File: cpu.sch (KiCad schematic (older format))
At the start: 28 parts, among them P27 BDM, U1 MC9S12XDP512, X1 16MHz

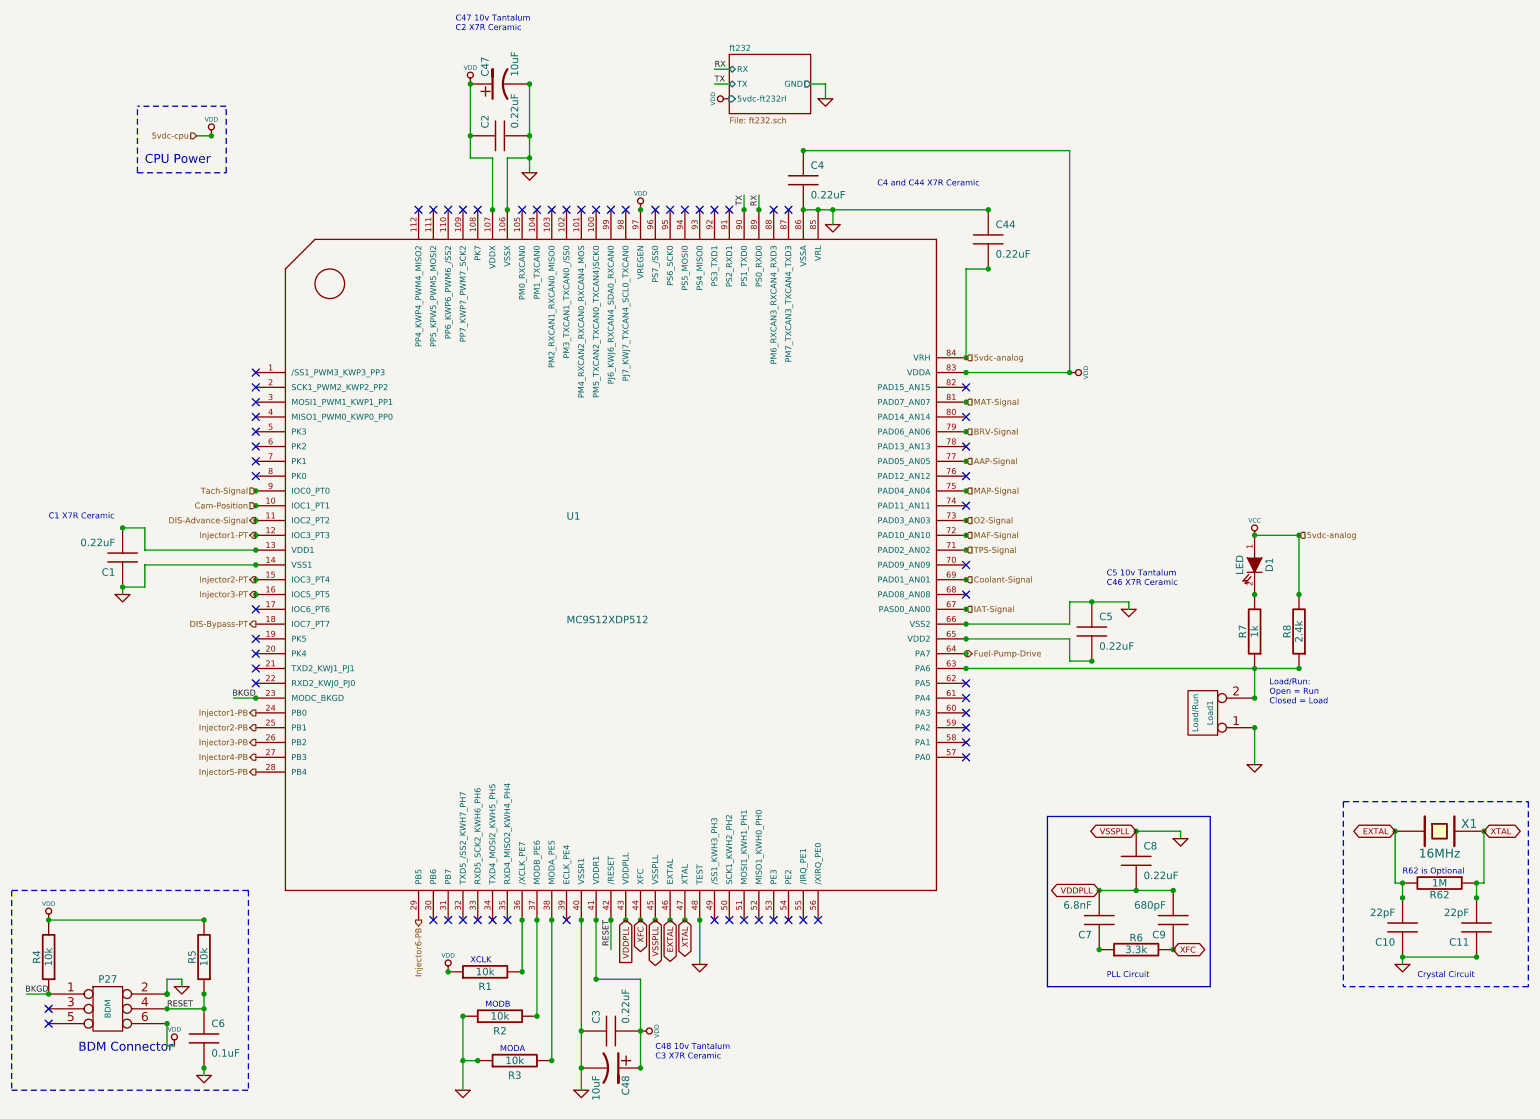
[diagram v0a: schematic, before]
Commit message: Updated Schematics, PDF, BOM for 4cyl Sequential Injection
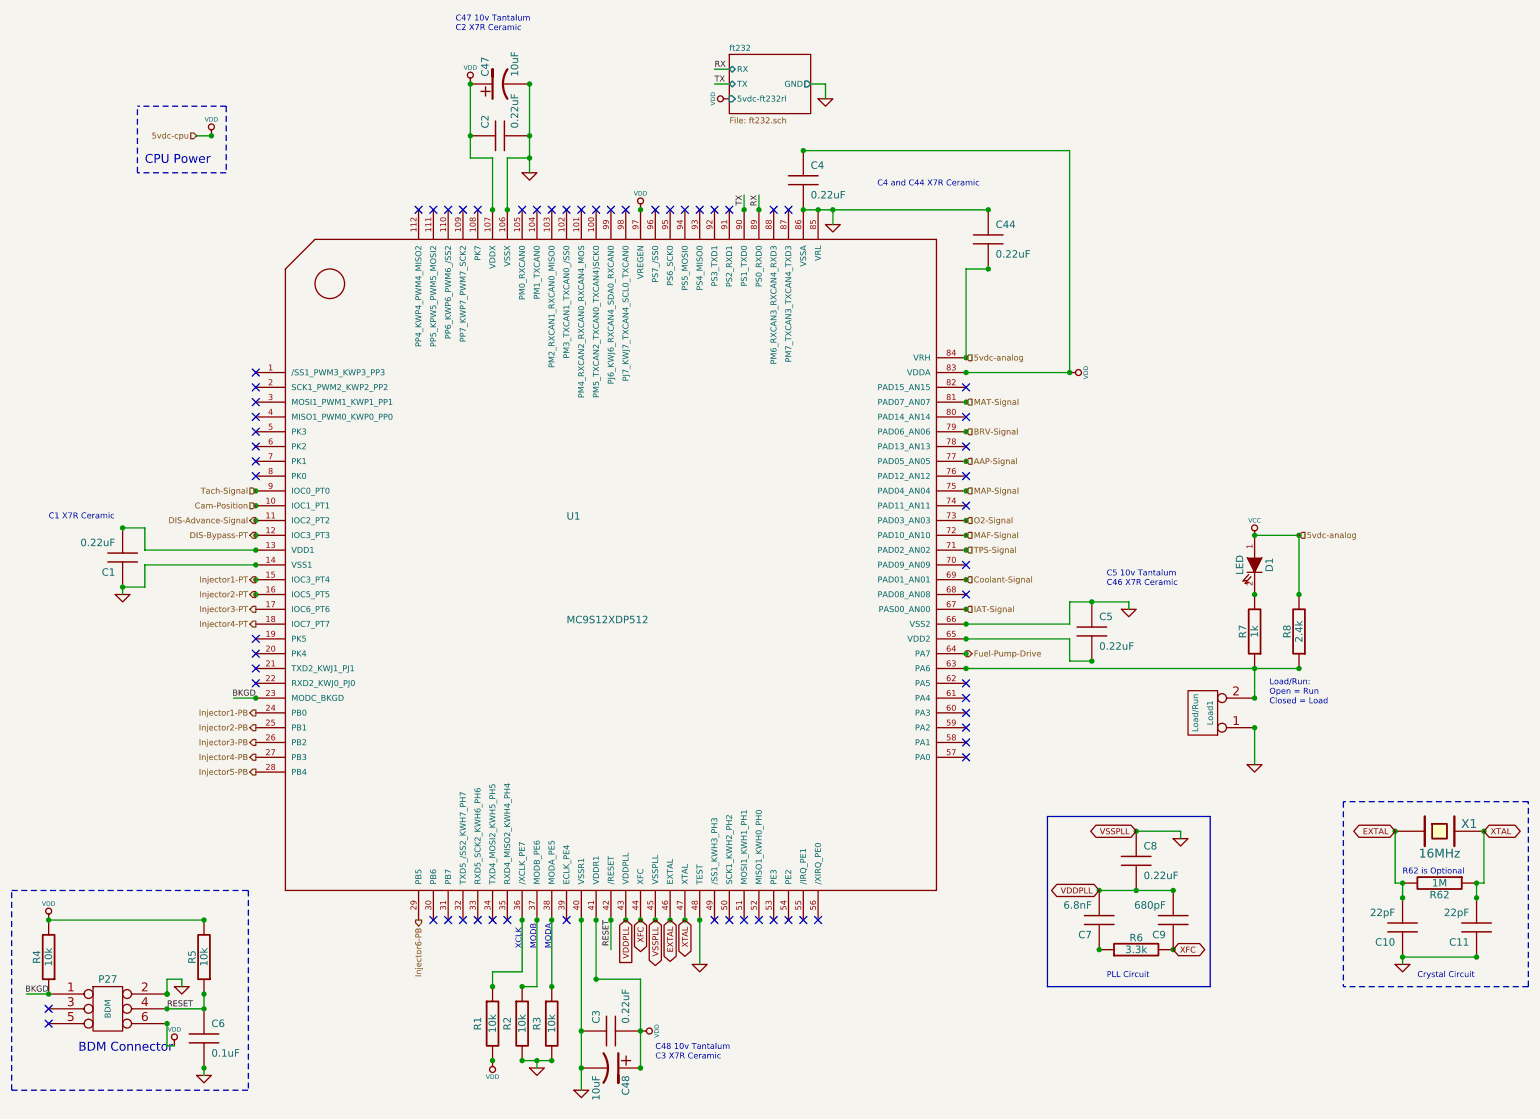
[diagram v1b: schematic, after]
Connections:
- net labels added: Injector4-PT
- wire segments 72 -> 75
- no-connect marks 64 -> 63
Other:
- moved on the sheet: R1, R2, R3

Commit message: Updated everything for up to 8 cylinder engines
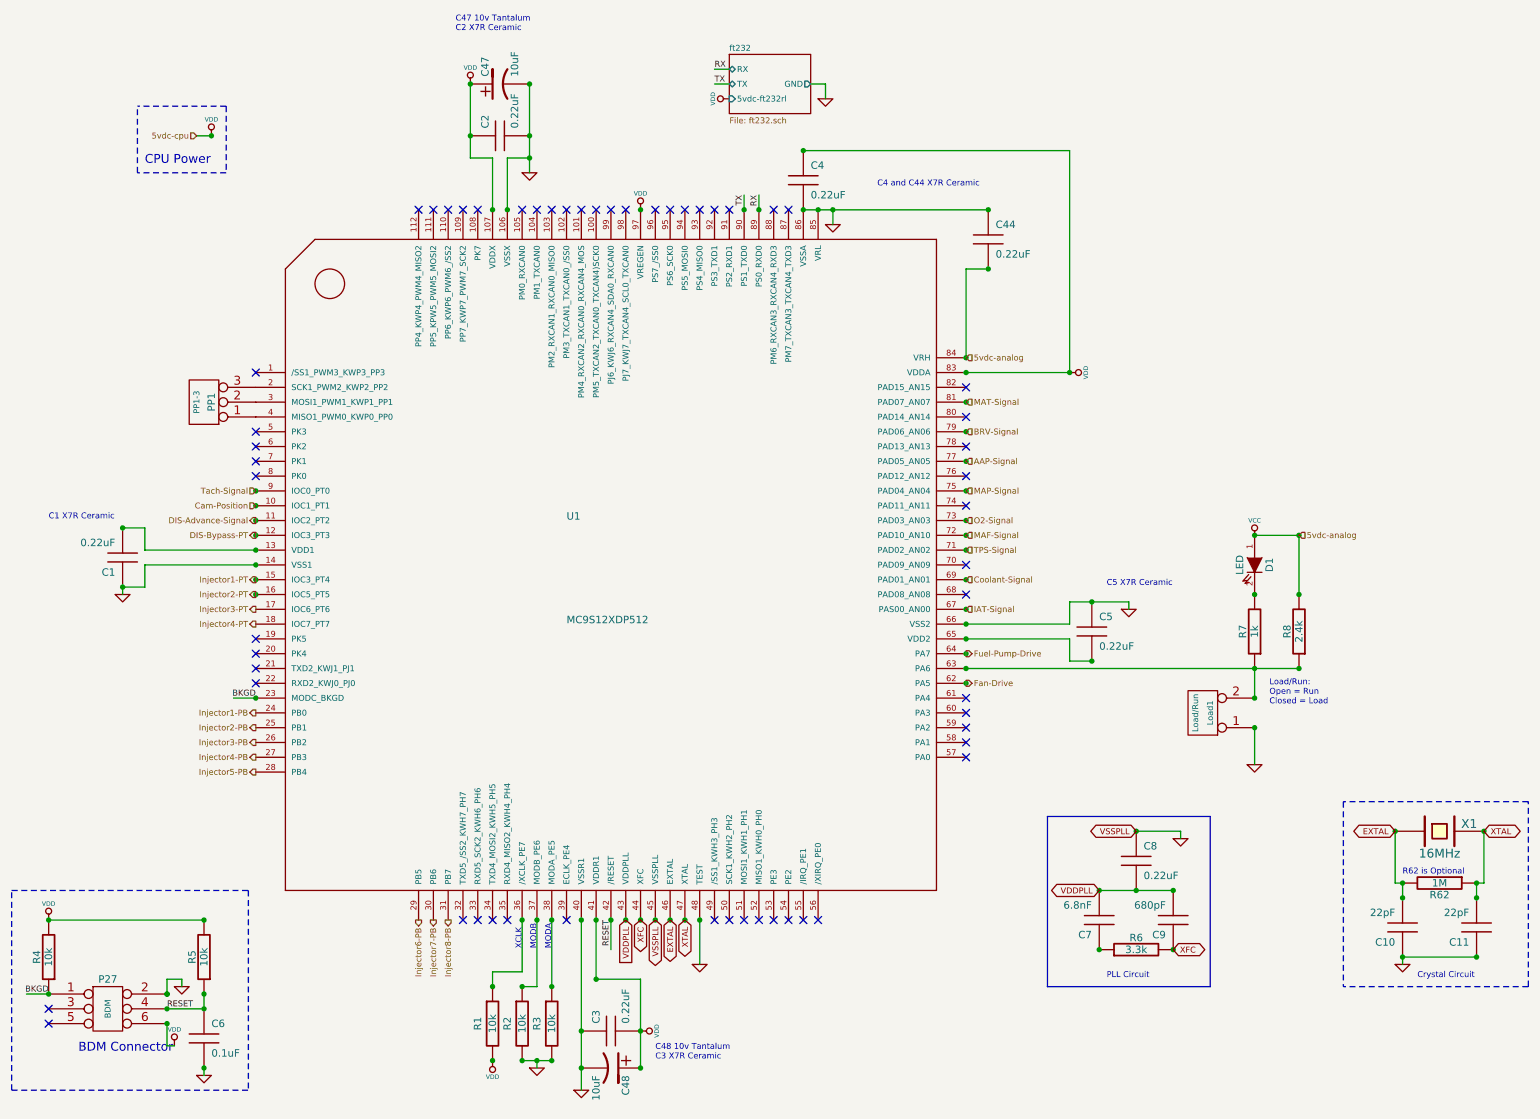
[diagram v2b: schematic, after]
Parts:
- added PP1: PP1-3, symbol CONN_3
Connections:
- net labels added: Fan-Drive, Injector7-PB, Injector8-PB
- no-connect marks 63 -> 57
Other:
- note added: "C5 X7R Ceramic"
- note removed: "C5 10v Tantalum\nC46 X7R Ceramic"
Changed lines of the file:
@@
-EESchema Schematic File Version 2  date Tue 24 Jan 2012 11:15:10 PM EST
+EESchema Schematic File Version 2  date Thu 26 Jan 2012 03:16:21 AM EST
 LIBS:power
 LIBS:device
@@
 Sheet 2 7
 Title "Jaguar PCB for FreeEMS"
-Date "25 jan 2012"
+Date "26 jan 2012"
 Rev "A.1"
 Comp "diyefi.org"
@@
 Comment4 ""
 $EndDescr
+$Comp
+L CONN_3 PP1
+U 1 1 4F210899
+P 1850 3050
+F 0 "PP1" V 1800 3050 50  0000 C CNN
+F 1 "PP1-3" V 1900 3050 40  0000 C CNN
+	1    1850 3050
+	-1   0    0    1
+$EndComp
+NoConn ~ 7000 5050
+Connection ~ 2200 3950
+NoConn ~ 7000 5450
+Connection ~ 7000 4950
+Text HLabel 7000 4950 2    40   Output ~ 0
+Fan-Drive
+Text HLabel 3500 6550 3    40   Output ~ 0
+Injector8-PB
+Text HLabel 3400 6550 3    40   Output ~ 0
+Injector7-PB
 Connection ~ 4200 7500
 Connection ~ 4000 7500
@@
 Connection ~ 2200 4350
 Connection ~ 2200 4250
-Connection ~ 2200 3950
 Connection ~ 2200 3850
 Connection ~ 2200 3750
@@
 C1 X7R Ceramic
 Text Notes 7950 4300 0    40   ~ 0
-C5 10v Tantalum\nC46 X7R Ceramic
+C5 X7R Ceramic
 $Comp
 L CONN_2 Load1
@@
 $EndComp
 $Comp
-L GND #PWR03
+L GND #PWR02
 U 1 1 4F1D6CA4
 P 1300 4350
-F 0 "#PWR03" H 1300 4350 30  0001 C CNN
+F 0 "#PWR02" H 1300 4350 30  0001 C CNN
 F 1 "GND" H 1300 4280 30  0001 C CNN
 	1    1300 4350
@@
 5vdc-analog
 $Comp
-L VCC #PWR04
+L VCC #PWR03
 U 1 1 4F1CE2A5
 P 8950 3950
-F 0 "#PWR04" H 8950 4050 30  0001 C CNN
+F 0 "#PWR03" H 8950 4050 30  0001 C CNN
 F 1 "VCC" H 8950 4050 30  0000 C CNN
 	1    8950 3950
@@
 $EndComp
 $Comp
-L VDD #PWR05
+L VDD #PWR04
 U 1 1 4F1C3492
 P 5400 1000
-F 0 "#PWR05" H 5400 1100 30  0001 C CNN
+F 0 "#PWR04" H 5400 1100 30  0001 C CNN
 F 1 "VDD" H 5400 1110 30  0000 C CNN
 	1    5400 1000
@@
 $EndComp
 $Comp
-L VDD #PWR06
+L VDD #PWR05
 U 1 1 4F1C343C
 P 1650 7400
-F 0 "#PWR06" H 1650 7500 30  0001 C CNN
+F 0 "#PWR05" H 1650 7500 30  0001 C CNN
 F 1 "VDD" H 1650 7510 30  0000 C CNN
 	1    1650 7400
@@
 $EndComp
 $Comp
-L VDD #PWR07
+L VDD #PWR06
 U 1 1 4F1C31B7
 P 800 6550
-F 0 "#PWR07" H 800 6650 30  0001 C CNN
+F 0 "#PWR06" H 800 6650 30  0001 C CNN
 F 1 "VDD" H 800 6660 30  0000 C CNN
 	1    800  6550
@@
 $EndComp
 $Comp
-L VDD #PWR08
+L VDD #PWR07
 U 1 1 4F1C31AA
 P 3800 7500
-F 0 "#PWR08" H 3800 7600 30  0001 C CNN
+F 0 "#PWR07" H 3800 7600 30  0001 C CNN
 F 1 "VDD" H 3800 7610 30  0000 C CNN
 	1    3800 7500
@@
 $EndComp
 $Comp
-L VDD #PWR09
+L VDD #PWR08
 U 1 1 4F1C3179
 P 4800 7300
-F 0 "#PWR09" H 4800 7400 30  0001 C CNN
+F 0 "#PWR08" H 4800 7400 30  0001 C CNN
 F 1 "VDD" H 4800 7410 30  0000 C CNN
 	1    4800 7300
@@
 $EndComp
 $Comp
-L GND #PWR010
+L GND #PWR09
 U 1 1 4F1C316A
 P 5200 6850
-F 0 "#PWR010" H 5200 6850 30  0001 C CNN
+F 0 "#PWR09" H 5200 6850 30  0001 C CNN
 F 1 "GND" H 5200 6780 30  0001 C CNN
 	1    5200 6850
@@
 $EndComp
 $Comp
-L GND #PWR011
+L GND #PWR010
 U 1 1 4F1C3153
 P 8450 6000
-F 0 "#PWR011" H 8450 6000 30  0001 C CNN
+F 0 "#PWR010" H 8450 6000 30  0001 C CNN
 F 1 "GND" H 8450 5930 30  0001 C CNN
 	1    8450 6000
@@
 $EndComp
 $Comp
-L VDD #PWR012
+L VDD #PWR011
 U 1 1 4F1C3124
 P 7700 2850
-F 0 "#PWR012" H 7700 2950 30  0001 C CNN
+F 0 "#PWR011" H 7700 2950 30  0001 C CNN
 F 1 "VDD" H 7700 2960 30  0000 C CNN
 	1    7700 2850
@@
 $EndComp
 $Comp
-L VDD #PWR013
+L VDD #PWR012
 U 1 1 4F1C3115
 P 4800 1750
-F 0 "#PWR013" H 4800 1850 30  0001 C CNN
+F 0 "#PWR012" H 4800 1850 30  0001 C CNN
 F 1 "VDD" H 4800 1860 30  0000 C CNN
 	1    4800 1750
@@
 $EndComp
 $Comp
-L VDD #PWR014
+L VDD #PWR013
 U 1 1 4F1C30FA
 P 1900 1250
-F 0 "#PWR014" H 1900 1350 30  0001 C CNN
+F 0 "#PWR013" H 1900 1350 30  0001 C CNN
 F 1 "VDD" H 1900 1360 30  0000 C CNN
 	1    1900 1250
@@
 $EndComp
 $Comp
-L VDD #PWR015
+L VDD #PWR014
 U 1 1 4F1C30DD
 P 3650 900
-F 0 "#PWR015" H 3650 1000 30  0001 C CNN
+F 0 "#PWR014" H 3650 1000 30  0001 C CNN
 F 1 "VDD" H 3650 1010 30  0000 C CNN
 	1    3650 900
@@
 $EndComp
 $Comp
-L GND #PWR016
+L GND #PWR015
 U 1 1 4F1C290C
 P 1700 7000
-F 0 "#PWR016" H 1700 7000 30  0001 C CNN
+F 0 "#PWR015" H 1700 7000 30  0001 C CNN
 F 1 "GND" H 1700 6930 30  0001 C CNN
 	1    1700 7000
@@
 $EndComp
 $Comp
-L GND #PWR017
+L GND #PWR016
 U 1 1 4F1C2905
 P 1850 7600
-F 0 "#PWR017" H 1850 7600 30  0001 C CNN
+F 0 "#PWR016" H 1850 7600 30  0001 C CNN
 F 1 "GND" H 1850 7530 30  0001 C CNN
 	1    1850 7600
@@
 $EndComp
 $Comp
-L GND #PWR018
+L GND #PWR017
 U 1 1 4F1C289E
 P 4050 1500
-F 0 "#PWR018" H 4050 1500 30  0001 C CNN
+F 0 "#PWR017" H 4050 1500 30  0001 C CNN
 F 1 "GND" H 4050 1430 30  0001 C CNN
 	1    4050 1500
@@
 $EndComp
 $Comp
-L GND #PWR019
+L GND #PWR018
 U 1 1 4F1C287C
 P 6050 1000
-F 0 "#PWR019" H 6050 1000 30  0001 C CNN
+F 0 "#PWR018" H 6050 1000 30  0001 C CNN
 F 1 "GND" H 6050 930 30  0001 C CNN
 	1    6050 1000
@@
 $EndComp
 $Comp
-L GND #PWR020
+L GND #PWR019
 U 1 1 4F1C2863
 P 6100 1850
-F 0 "#PWR020" H 6100 1850 30  0001 C CNN
+F 0 "#PWR019" H 6100 1850 30  0001 C CNN
 F 1 "GND" H 6100 1780 30  0001 C CNN
 	1    6100 1850
@@
 $EndComp
 $Comp
-L GND #PWR021
+L GND #PWR020
 U 1 1 4F1C284A
 P 8950 5500
-F 0 "#PWR021" H 8950 5500 30  0001 C CNN
+F 0 "#PWR020" H 8950 5500 30  0001 C CNN
 F 1 "GND" H 8950 5430 30  0001 C CNN
 	1    8950 5500
@@
 $EndComp
 $Comp
-L GND #PWR022
+L GND #PWR021
 U 1 1 4F1C2831
 P 8100 4450
-F 0 "#PWR022" H 8100 4450 30  0001 C CNN
+F 0 "#PWR021" H 8100 4450 30  0001 C CNN
 F 1 "GND" H 8100 4380 30  0001 C CNN
 	1    8100 4450
@@
 $EndComp
 $Comp
-L GND #PWR023
+L GND #PWR022
 U 1 1 4F1C2808
 P 9950 6850
-F 0 "#PWR023" H 9950 6850 30  0001 C CNN
+F 0 "#PWR022" H 9950 6850 30  0001 C CNN
 F 1 "GND" H 9950 6780 30  0001 C CNN
 	1    9950 6850
@@
 XCLK
 $Comp
-L GND #PWR024
+L GND #PWR023
 U 1 1 4F1C2798
 P 4400 7700
-F 0 "#PWR024" H 4400 7700 30  0001 C CNN
+F 0 "#PWR023" H 4400 7700 30  0001 C CNN
 F 1 "GND" H 4400 7630 30  0001 C CNN
 	1    4400 7700
@@
 $EndComp
 $Comp
-L GND #PWR025
+L GND #PWR024
 U 1 1 4F1C273A
 P 4100 7550
-F 0 "#PWR025" H 4100 7550 30  0001 C CNN
+F 0 "#PWR024" H 4100 7550 30  0001 C CNN
 F 1 "GND" H 4100 7480 30  0001 C CNN
 	1    4100 7550
@@
 Text HLabel 2200 3650 0    40   Input ~ 0
 Tach-Signal
-NoConn ~ 3400 6550
-NoConn ~ 3500 6550
 $Comp
 L MC9S12XDP512 U1
@@
 $EndSheet
 NoConn ~ 2200 2850
-NoConn ~ 2200 2950
-NoConn ~ 2200 3050
-NoConn ~ 2200 3150
 NoConn ~ 2200 3250
 NoConn ~ 2200 3350
@@
 NoConn ~ 5900 6550
 NoConn ~ 6000 6550
-NoConn ~ 7000 5450
 NoConn ~ 7000 5350
 NoConn ~ 7000 5250
 NoConn ~ 7000 5150
-NoConn ~ 7000 5050
-NoConn ~ 7000 4950
 NoConn ~ 7000 4150
 NoConn ~ 7000 3750
